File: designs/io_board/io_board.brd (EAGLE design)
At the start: 160 x 100 mm, 47 parts, among them U6 MSP430FR5739IDA

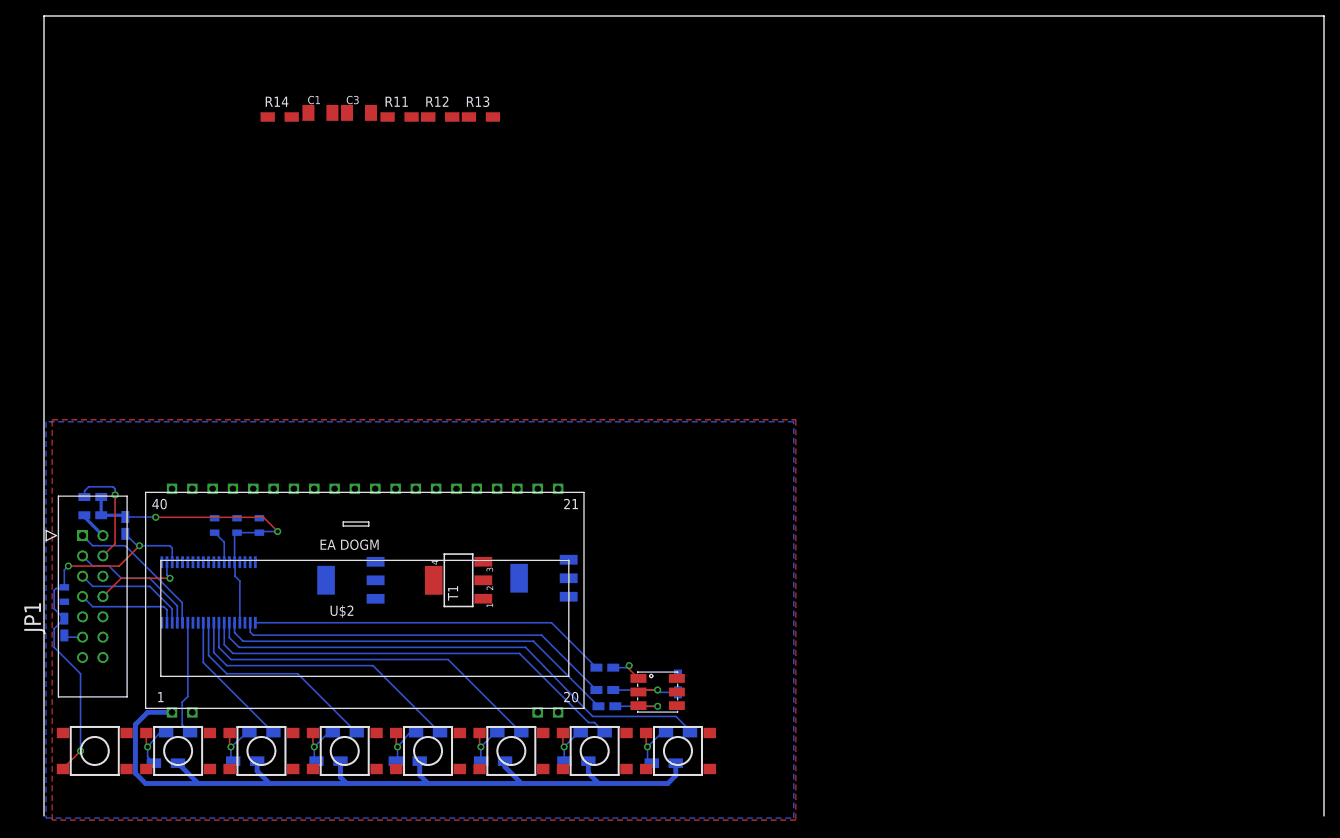
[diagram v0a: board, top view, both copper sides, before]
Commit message: Adding bord file for lcd screen
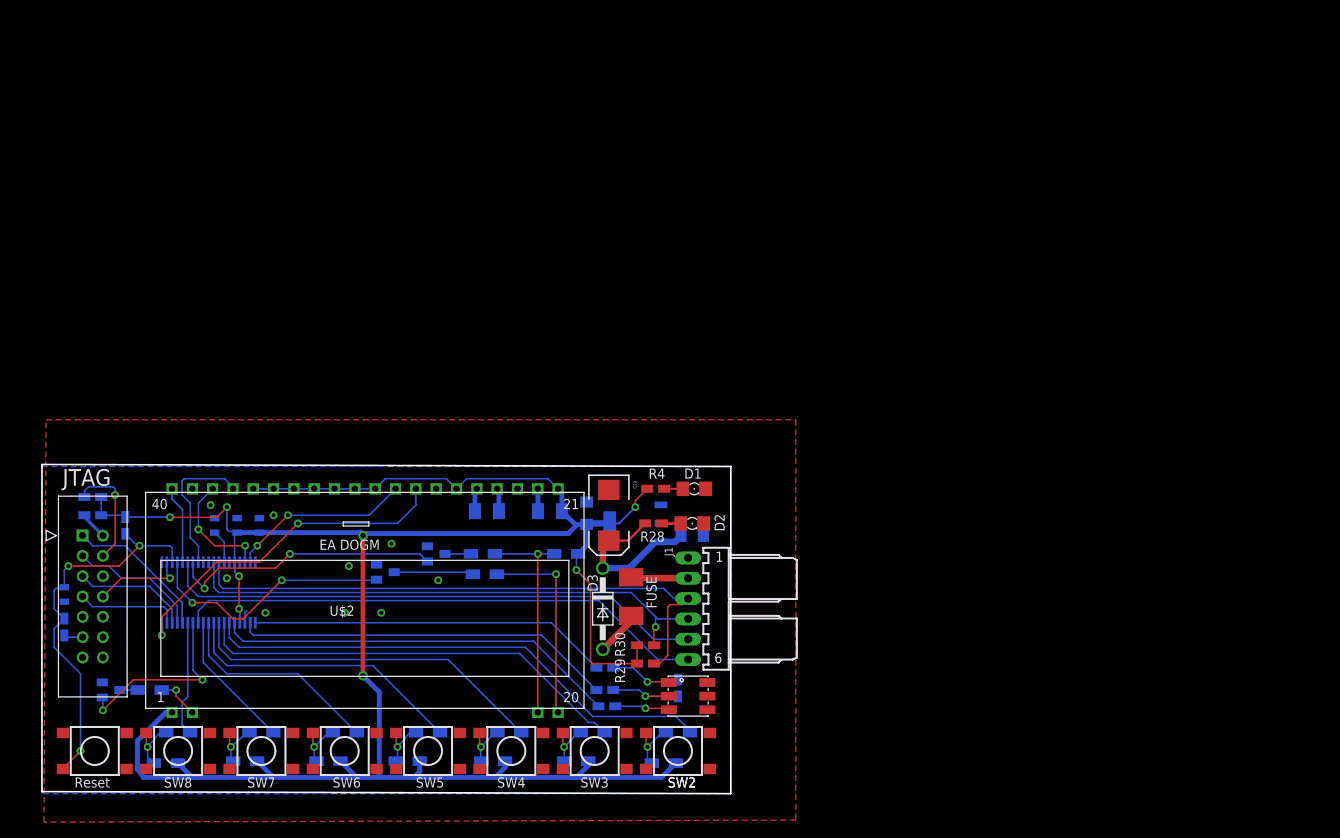
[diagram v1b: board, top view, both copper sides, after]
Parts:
- added C10, C11: 10uF, SparkFun-Capacitors:EIA3216
- added C22: 100uF, SparkFun-Capacitors:EIA7343
- added D1: 3_3V_PWR, SparkFun-LED:FKIT-LED-1206
- added D2: 5V_PWR, SparkFun-LED:FKIT-LED-1206
- added D3: 1N4004, diode:DO41-10
- added J1: 22-05-7068-06, con-molex:7395-06
- added R28, R4: 330, rcl:R0805W
- added R29, R30: 4.7k, rcl:R0805W
- added U$3: NANO_FUSE, custom_fuses:NANO_FUSE
- added U5: LMS8117AMP-3.3, NSC-LMS8117AMP:SOT230P696X180-4N
- R10, R11, R12, R13, R15, R16, R17, R18, R19, R20, R21, R22, R23, R24, R25, R26, R27: value (none) -> 10k
- T1, T2, T3: value (none) -> BSS123; device zetex:SOT223 -> transistor-small-signal:SOT23
- moved R11 78.1 mm to (13.2, 15.7), flipped to the bottom, turned to 180 degrees
- moved R14 65.3 mm to (65.3, 32.8), flipped to the bottom
- moved C1 57.5 mm to (63.2, 38.1), flipped to the bottom
- moved R13 57.2 mm to (55.1, 30.2), flipped to the bottom, turned to 180 degrees
- moved T2 55.9 mm to (8.38, 15.7), turned to 90 degrees
- moved R12 54.9 mm to (54.9, 32.8), flipped to the bottom, turned to 180 degrees
- moved C3 52.3 mm to (55.4, 38.1), flipped to the bottom, turned to 180 degrees
- moved T3 4.44 mm to (42.7, 30.5), turned to 90 degrees
- moved T1 4.33 mm to (49.0, 32.8), flipped to the bottom
- moved U$7 3.84 mm to (80.5, 15.0)
- moved R3 0.51 mm to (79.2, 16.0)
- renumbered JP1 to JTAG
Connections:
- removed net +3V3: C1.1, R10.2, R14.1, R15.2, R16.2, R17.2, R18.2, R19.2, R20.2, U$2.1, U$2.21, U$2.26, U$2.30, U$2.31, U$2.32, U$2.33, U$2.34, U$2.35, U$2.36
- removed net 3.3V: C14.1, C15.1, R6.2, R7.2, R9.2, U6.34, U6.4
- removed net CLK: U$2.29
- removed net MISO: U6.20
- removed net MOSI: U6.19
- removed net SI: U$2.28
- new net LCD_CLK: U$2.29, U6.37
- new net LCD_SIMO: U$2.28, U6.19
- new net N$23: D1.A, R4.2
- new net N$24: D2.A, R28.1
- new net N$25: D3.A, U$3.2
- new net N$27: C10.A, C22.A, D3.C, R28.2, U5.3
- new net SIMO_SDA: J1.4, R30.1, U6.30
- new net SOMI_SCL: J1.3, R29.1, U6.31
- new net SPI_CLK: J1.5, U6.25
- new net SPI_EN: J1.6, U6.12
- new net VCC: C1.1, C11.A, C14.1, C15.1, R10.2, R14.1, R15.2, R16.2, R17.2, R18.2, R19.2, R20.2, R29.2, R30.2, R4.1, R6.2, R7.2, R9.2, U$2.1, U$2.21, U$2.26, U$2.30, U$2.31, U$2.32, U$2.33, U$2.34, U$2.35, U$2.36, U5.4, U6.34, U6.4
- new net VCC5: J1.2, U$3.1
- net BLUE: now also U6.23
- net CSB: now also U6.36
- net GND: now also C10.C, C11.C, C22.C, D1.C, D2.C, J1.1, T1.2, T2.2, T3.2, U5.1; no longer T1.3, T2.3, T3.3
- net GREEN: now also U6.26
- net N$2: now also T2.3; no longer T2.2, T2.4
- net N$3: now also T1.3; no longer T1.2, T1.4
- net N$7: now also T3.3; no longer T3.2, T3.4
- net R/W: now also U6.27
- net RED: now also U6.13
- net RESET_LCD: now also U6.24
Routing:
- net VCC: track 0.00 -> 286.1 mm, vias 0 -> 8
- net +3V3: track 101.7 -> 0.00 mm
- net SOMI_SCL: track 0.00 -> 73.4 mm
- net SPI_CLK: track 0.00 -> 68.3 mm
- net SIMO_SDA: track 0.00 -> 67.7 mm, vias 0 -> 1
- net SPI_EN: track 0.00 -> 66.3 mm
- net LCD_SIMO: track 0.00 -> 43.4 mm, vias 0 -> 2
- net 3.3V: track 42.0 -> 0.00 mm, vias 2 -> 0
- net GREEN: track 0.00 -> 34.4 mm, vias 0 -> 2
- net BLUE: track 0.00 -> 31.7 mm, vias 0 -> 2
- net N$1: track 0.00 -> 27.2 mm, vias 0 -> 1
- net N$10: track 0.00 -> 24.8 mm, vias 0 -> 1
- net RED: track 0.00 -> 23.3 mm, vias 0 -> 2
- net LCD_CLK: track 0.00 -> 22.6 mm, vias 0 -> 2
- net N$27: track 0.00 -> 20.6 mm
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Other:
- board size 160 x 100 mm -> 86.1 x 41.1 mm
- board text added: "Reset"
- board text added: "SW2"
- board text added: "SW3"
- board text added: "SW4"
- board text added: "SW5"
- board text added: "SW6"
- board text added: "SW7"
- board text added: "SW8"
